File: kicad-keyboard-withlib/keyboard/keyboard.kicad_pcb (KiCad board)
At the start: 2 copper layers, 149.1 x 131.9 mm, 54 parts, among them SW1 SW_Push, SW10 SW_Push, SW11 SW_Push, SW12 SW_Push, SW13 SW_Push, SW14 SW_Push, SW15 SW_Push, SW16 SW_Push, SW17 SW_Push, SW18 SW_Push, SW19 SW_Push, SW2 SW_Push, SW20 SW_Push, SW21 SW_Push, SW22 SW_Push, SW23 SW_Push, SW24 SW_Push, SW25 SW_Push, SW26 SW_Push, SW27 SW_Push, SW28 SW_Push, SW29 SW_Push, SW3 SW_Push, SW30 SW_Push, SW31 SW_Push, SW32 SW_Push, SW33 SW_Push, SW34 SW_Push, SW35 SW_Push, SW36 SW_Push, SW37 SW_Push, SW38 SW_Push, SW39 SW_Slide_DPDT, SW4 SW_Push, SW5 SW_Push, SW6 SW_Push, SW7 SW_Push, SW8 SW_Push, SW9 SW_Push, U2 MCP23017_SO

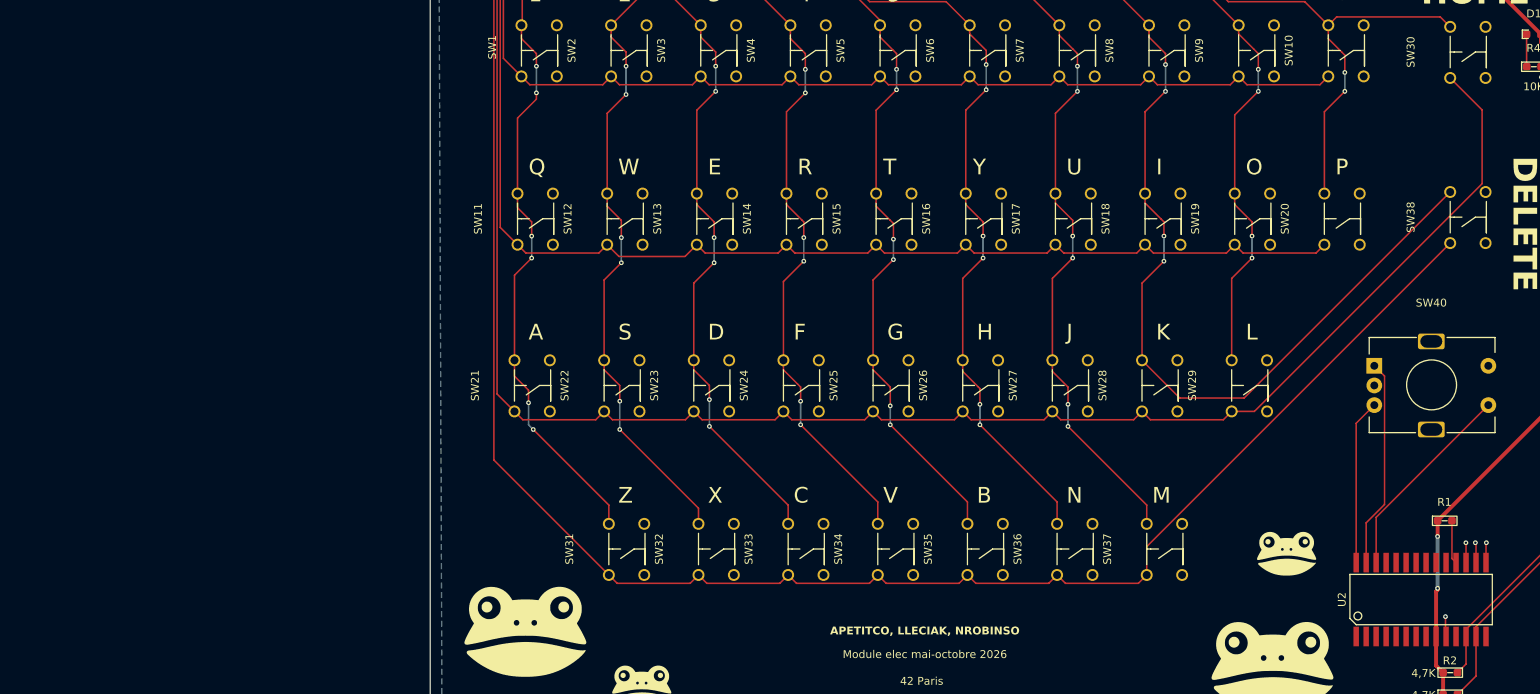
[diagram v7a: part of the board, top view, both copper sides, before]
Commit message: add: started the pcb with diode, add the 10k missing comments silkscreen
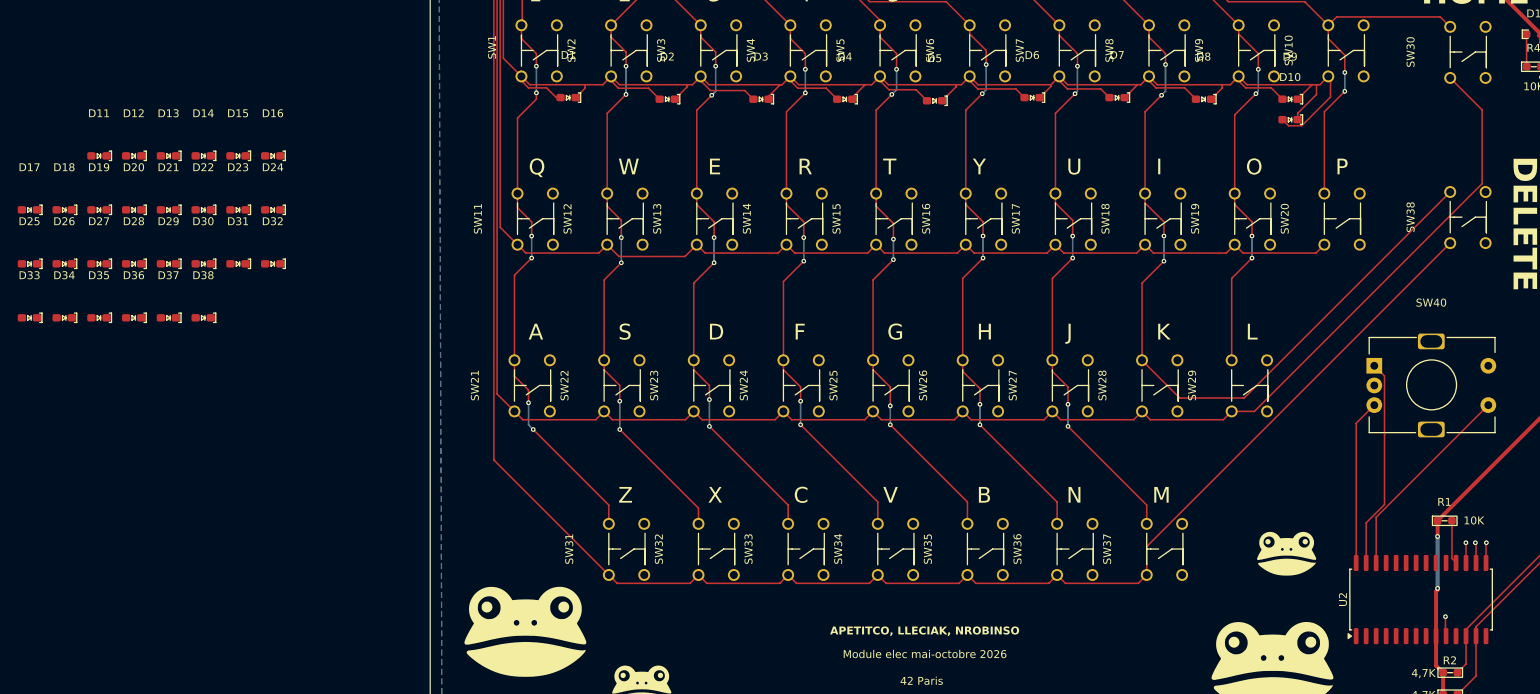
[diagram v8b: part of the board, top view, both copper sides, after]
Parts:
- added D1: ~, Lilyspad:diode, F.Cu at (40.0, 80.1)
- added D10: ~, Lilyspad:diode, F.Cu at (131.8, 82.9)
- added D11: ~, Lilyspad:diode, F.Cu at (-19.6, 87.5)
- added D12: ~, Lilyspad:diode, F.Cu at (-15.2, 87.5)
- added D13: ~, Lilyspad:diode, F.Cu at (-10.8, 87.5)
- added D14: ~, Lilyspad:diode, F.Cu at (-6.36, 87.5)
- added D15: ~, Lilyspad:diode, F.Cu at (-1.94, 87.5)
- added D16: ~, Lilyspad:diode, F.Cu at (2.48, 87.5)
- added D17: ~, Lilyspad:diode, F.Cu at (-28.5, 94.4)
- added D18: ~, Lilyspad:diode, F.Cu at (-24.0, 94.4)
- added D19: ~, Lilyspad:diode, F.Cu at (-19.6, 94.4)
- added D2: ~, Lilyspad:diode, F.Cu at (52.6, 80.3)
- added D20: ~, Lilyspad:diode, F.Cu at (-15.2, 94.4)
- added D21: ~, Lilyspad:diode, F.Cu at (-10.8, 94.4)
- added D22: ~, Lilyspad:diode, F.Cu at (-6.36, 94.4)
- added D23: ~, Lilyspad:diode, F.Cu at (-1.94, 94.4)
- added D24: ~, Lilyspad:diode, F.Cu at (2.48, 94.4)
- added D25: ~, Lilyspad:diode, F.Cu at (-28.5, 101.3)
- added D26: ~, Lilyspad:diode, F.Cu at (-24.0, 101.3)
- added D27: ~, Lilyspad:diode, F.Cu at (-19.6, 101.3)
- added D28: ~, Lilyspad:diode, F.Cu at (-15.2, 101.3)
- added D29: ~, Lilyspad:diode, F.Cu at (-10.8, 101.3)
- added D3: ~, Lilyspad:diode, F.Cu at (64.6, 80.3)
- added D30: ~, Lilyspad:diode, F.Cu at (-6.36, 101.3)
- added D31: ~, Lilyspad:diode, F.Cu at (-1.94, 101.3)
- added D32: ~, Lilyspad:diode, F.Cu at (2.48, 101.3)
- added D33: ~, Lilyspad:diode, F.Cu at (-28.5, 108.1)
- added D34: ~, Lilyspad:diode, F.Cu at (-24.0, 108.1)
- added D35: ~, Lilyspad:diode, F.Cu at (-19.6, 108.1)
- added D36: ~, Lilyspad:diode, F.Cu at (-15.2, 108.1)
- added D37: ~, Lilyspad:diode, F.Cu at (-10.8, 108.1)
- added D38: ~, Lilyspad:diode, F.Cu at (-6.36, 108.1)
- added D4: ~, Lilyspad:diode, F.Cu at (75.2, 80.3)
- added D5: ~, Lilyspad:diode, F.Cu at (86.6, 80.5)
- added D6: ~, Lilyspad:diode, F.Cu at (99.0, 80.1)
- added D7: ~, Lilyspad:diode, F.Cu at (109.8, 80.1)
- added D8: ~, Lilyspad:diode, F.Cu at (120.8, 80.3)
- added D9: ~, Lilyspad:diode, F.Cu at (131.8, 80.3)
- U2: footprint Lilyspad:MCP23017 -> Package_SO:SOIC-28W_7.5x17.9mm_P1.27mm
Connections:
- R4 pad 1: Net-(D1-K) -> Net-(R4-Pad1)
- SW1 pad 1: Net-(U1-R1) -> Net-(D1-Pad1)
- SW10 pad 1: Net-(U1-R1) -> Net-(D10-Pad1)
- SW11 pad 1: Net-(U1-R2) -> Net-(D11-Pad1)
- SW12 pad 1: Net-(U1-R2) -> Net-(D12-Pad1)
- SW13 pad 1: Net-(U1-R2) -> Net-(D13-Pad1)
- SW14 pad 1: Net-(U1-R2) -> Net-(D14-Pad1)
- SW15 pad 1: Net-(U1-R2) -> Net-(D15-Pad1)
- SW16 pad 1: Net-(U1-R2) -> Net-(D16-Pad1)
- SW17 pad 1: Net-(U1-R2) -> Net-(D17-Pad1)
- SW18 pad 1: Net-(U1-R2) -> Net-(D18-Pad1)
- SW19 pad 1: Net-(U1-R2) -> Net-(D19-Pad1)
- SW2 pad 1: Net-(U1-R1) -> Net-(D2-Pad1)
- SW20 pad 1: Net-(U1-R2) -> Net-(D20-Pad1)
- SW21 pad 1: Net-(U1-R3) -> Net-(D21-Pad1)
- SW22 pad 1: Net-(U1-R3) -> Net-(D22-Pad1)
- SW23 pad 1: Net-(U1-R3) -> Net-(D23-Pad1)
- SW24 pad 1: Net-(U1-R3) -> Net-(D24-Pad1)
- SW25 pad 1: Net-(U1-R3) -> Net-(D25-Pad1)
- SW26 pad 1: Net-(U1-R3) -> Net-(D26-Pad1)
- SW27 pad 1: Net-(U1-R3) -> Net-(D27-Pad1)
- SW28 pad 1: Net-(U1-R3) -> Net-(D28-Pad1)
- SW29 pad 1: Net-(U1-R3) -> Net-(D29-Pad1)
- SW3 pad 1: Net-(U1-R1) -> Net-(D3-Pad1)
- SW30 pad 1: Net-(U1-R3) -> Net-(D30-Pad1)
- SW31 pad 1: Net-(U1-R4) -> Net-(D31-Pad1)
- SW32 pad 1: Net-(U1-R4) -> Net-(D32-Pad1)
- SW33 pad 1: Net-(U1-R4) -> Net-(D33-Pad1)
- SW34 pad 1: Net-(U1-R4) -> Net-(D34-Pad1)
- SW35 pad 1: Net-(U1-R4) -> Net-(D35-Pad1)
- SW36 pad 1: Net-(U1-R4) -> Net-(D36-Pad1)
- SW37 pad 1: Net-(U1-R4) -> Net-(D37-Pad1)
- SW38 pad 1: Net-(U1-R4) -> Net-(D38-Pad1)
- SW4 pad 1: Net-(U1-R1) -> Net-(D4-Pad1)
- SW40 pad D: GND -> (no net)
- SW40 pad E: Net-(U2-GPA5) -> (no net)
- SW5 pad 1: Net-(U1-R1) -> Net-(D5-Pad1)
- SW6 pad 1: Net-(U1-R1) -> Net-(D6-Pad1)
- SW7 pad 1: Net-(U1-R1) -> Net-(D7-Pad1)
- SW8 pad 1: Net-(U1-R1) -> Net-(D8-Pad1)
- SW9 pad 1: Net-(U1-R1) -> Net-(D9-Pad1)
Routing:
- net Net-(U1-R1): track 148.5 -> 175.9 mm
- net Net-(D10-Pad1): track 0.00 -> 10.3 mm
- net Net-(D6-Pad1): track 0.00 -> 7.86 mm
- net Net-(D3-Pad1): track 0.00 -> 7.67 mm
- net Net-(D7-Pad1): track 0.00 -> 7.26 mm
- net Net-(D2-Pad1): track 0.00 -> 7.14 mm
- net Net-(D5-Pad1): track 0.00 -> 7.02 mm
- net Net-(D8-Pad1): track 0.00 -> 6.94 mm
- net Net-(D4-Pad1): track 0.00 -> 6.92 mm
- net Net-(D9-Pad1): track 0.00 -> 6.54 mm
- net Net-(D1-Pad1): track 0.00 -> 6.40 mm
